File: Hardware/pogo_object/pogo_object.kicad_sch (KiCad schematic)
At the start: 32 parts, among them J1 10132797-035100LF, J2 10132797-015100LF, J3 Conn_01x02_Male, J4 Conn_01x02_Male, J5 Conn_01x04_Male, U1 dfr0489, U2 BSR802NL6327HTSA1, U3 mcp1407, U4 BSR802NL6327HTSA1

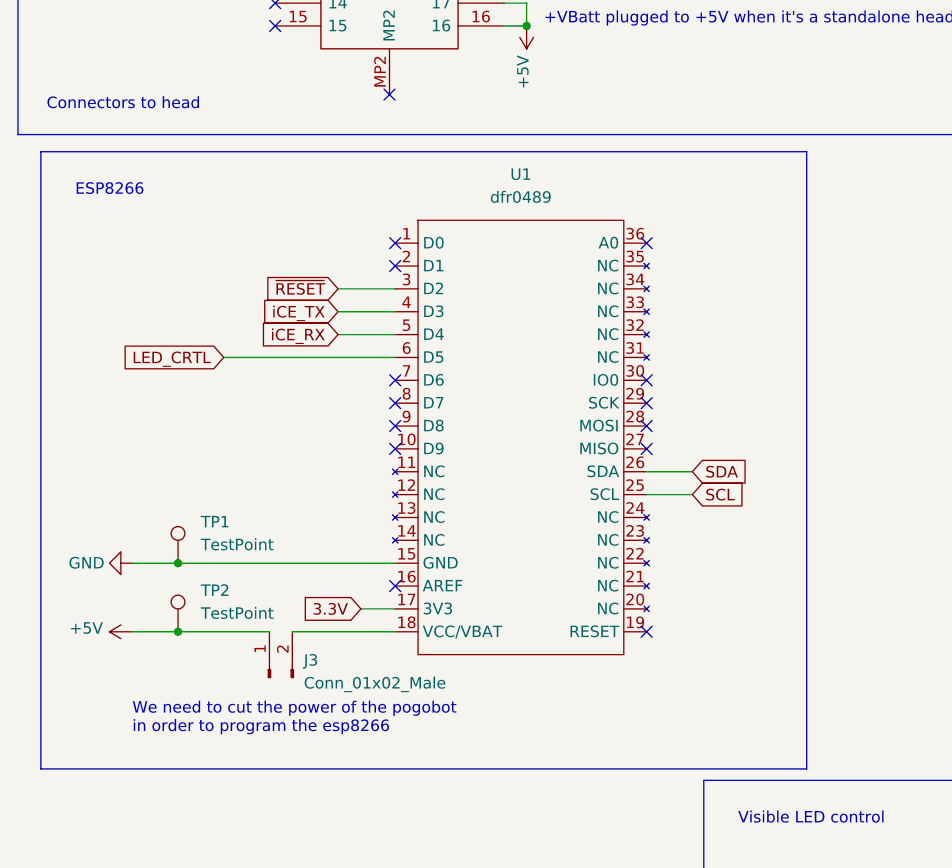
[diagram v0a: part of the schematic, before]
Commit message: adding battery voltage monitoring
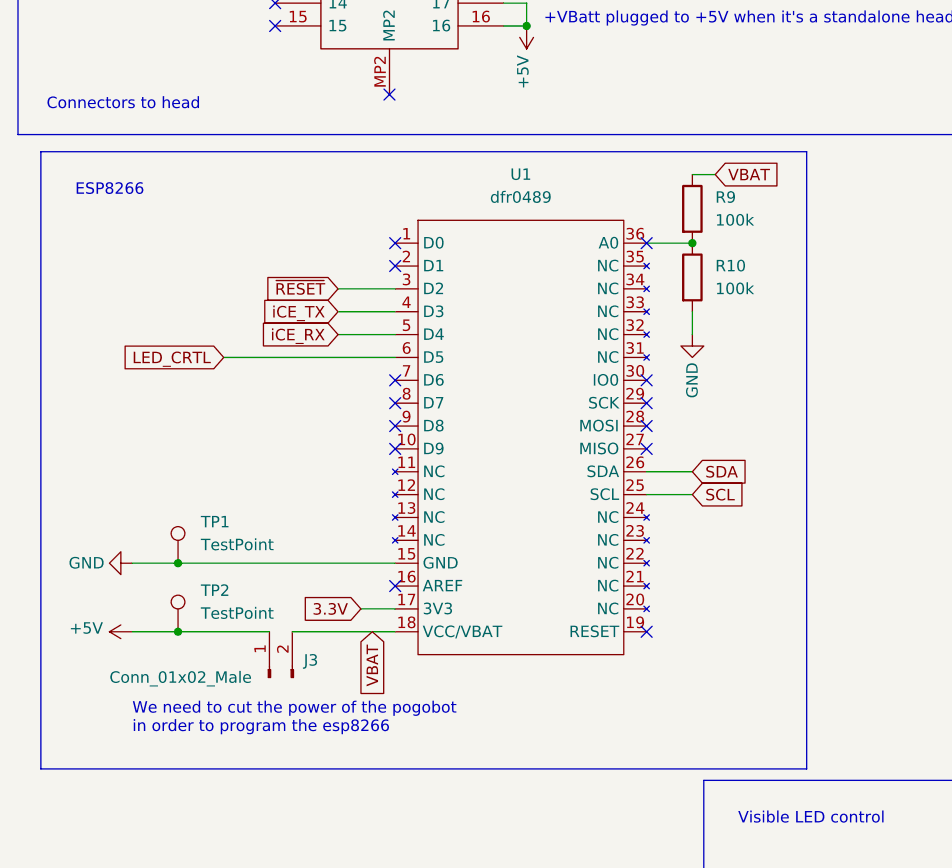
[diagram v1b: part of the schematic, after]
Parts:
- added R10, R9: 100k, Resistor_SMD:R_0805_2012Metric_Pad1.20x1.40mm_HandSolder, symbol Device:R
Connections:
- net GND: now also R10.2
- net VBAT: now reaches J3.2 (Pin_2), U1.18 (VCC/VBAT)
- net VBAT: now also R9.1
- net at U1.36 (A0): now also R10.1, R9.2
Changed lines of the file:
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@@
   (junction (at 31.75 124.46) (diameter 0) (color 0 0 0 0)
+  )
+  (junction (at 88.9 88.9) (diameter 0) (color 0 0 0 0)
   )
   (junction (at 201.93 113.03) (diameter 0) (color 0 0 0 0)
@@
     (stroke (width 0) (type default) (color 0 0 0 0))
   )
+  (wire (pts (xy 83.82 88.9) (xy 88.9 88.9))
+    (stroke (width 0) (type default) (color 0 0 0 0))
+  )
   (wire (pts (xy 76.2 31.75) (xy 67.945 31.75))
     (stroke (width 0) (type default) (color 0 0 0 0))
@@
     (stroke (width 0) (type default) (color 0 0 0 0))
   )
+  (wire (pts (xy 88.9 96.52) (xy 88.9 99.06))
+    (stroke (width 0) (type default) (color 0 0 0 0))
+  )
   (wire (pts (xy 76.2 36.83) (xy 67.945 36.83))
     (stroke (width 0) (type default) (color 0 0 0 0))
@@
   )
   (wire (pts (xy 31.75 132.08) (xy 41.91 132.08))
+    (stroke (width 0) (type default) (color 0 0 0 0))
+  )
+  (wire (pts (xy 88.9 81.28) (xy 91.44 81.28))
     (stroke (width 0) (type default) (color 0 0 0 0))
   )
@@
     )
   )
+  (global_label "VBAT" (shape input) (at 91.44 81.28 0) (fields_autoplaced)
+    (effects (font (size 1.27 1.27)) (justify left))
+    (property "Références Inter-Feuilles" "${INTERSHEET_REFS}" (id 0) (at 98.2679 81.3594 0)
+      (effects (font (size 1.27 1.27)) (justify left) hide)
+    )
+  )
   (global_label "SDA" (shape input) (at 185.42 31.75 0) (fields_autoplaced)
     (effects (font (size 1.27 1.27)) (justify left))
@@
     )
   )
+  (global_label "VBAT" (shape input) (at 53.34 132.08 270) (fields_autoplaced)
+    (effects (font (size 1.27 1.27)) (justify right))
+    (property "Références Inter-Feuilles" "${INTERSHEET_REFS}" (id 0) (at 53.2606 138.9079 90)
+      (effects (font (size 1.27 1.27)) (justify right) hide)
+    )
+  )
   (global_label "RGB_LED_IN" (shape input) (at 71.755 49.53 0) (fields_autoplaced)
     (effects (font (size 1.27 1.27)) (justify left))
@@
     )
     (property "Datasheet" "~" (id 3) (at 140.97 162.56 0)
+      (effects (font (size 1.27 1.27)) hide)
+    )
+    (pin "1")
+    (pin "2")
+  )
+  (symbol (lib_id "Device:R") (at 88.9 85.09 0) (unit 1)
+    (in_bom yes) (on_board yes) (fields_autoplaced)
+    (property "Reference" "R9" (id 0) (at 91.44 83.8199 0)
+      (effects (font (size 1.27 1.27)) (justify left))
+    )
+    (property "Value" "100k" (id 1) (at 91.44 86.3599 0)
+      (effects (font (size 1.27 1.27)) (justify left))
+    )
+    (property "Footprint" "Resistor_SMD:R_0805_2012Metric_Pad1.20x1.40mm_HandSolder" (id 2) (at 87.122 85.09 90)
+      (effects (font (size 1.27 1.27)) hide)
+    )
+    (property "Datasheet" "~" (id 3) (at 88.9 85.09 0)
       (effects (font (size 1.27 1.27)) hide)
     )
@@
     (pin "MP2")
   )
+  (symbol (lib_id "power:GND") (at 88.9 99.06 0) (mirror y) (unit 1)
+    (in_bom yes) (on_board yes)
+    (property "Reference" "#PWR014" (id 0) (at 88.9 105.41 0)
+      (effects (font (size 1.27 1.27)) hide)
+    )
+    (property "Value" "GND" (id 1) (at 88.9 104.14 90))
+    (property "Footprint" "" (id 2) (at 88.9 99.06 0)
+      (effects (font (size 1.27 1.27)) hide)
+    )
+    (property "Datasheet" "" (id 3) (at 88.9 99.06 0)
+      (effects (font (size 1.27 1.27)) hide)
+    )
+    (pin "1")
+  )
   (symbol (lib_id "Device:LED") (at 242.57 125.73 90) (unit 1)
     (in_bom yes) (on_board yes) (fields_autoplaced)
@@
   )
   (symbol (lib_id "Connector:Conn_01x02_Male") (at 41.91 137.16 90) (unit 1)
-    (in_bom yes) (on_board yes) (fields_autoplaced)
+    (in_bom yes) (on_board yes)
     (property "Reference" "J3" (id 0) (at 45.72 135.2549 90)
       (effects (font (size 1.27 1.27)) (justify right))
     )
-    (property "Value" "Conn_01x02_Male" (id 1) (at 45.72 137.7949 90)
+    (property "Value" "Conn_01x02_Male" (id 1) (at 24.13 137.16 90)
       (effects (font (size 1.27 1.27)) (justify right))
     )
@@
     (pin "1")
   )
+  (symbol (lib_id "Device:R") (at 88.9 92.71 0) (unit 1)
+    (in_bom yes) (on_board yes) (fields_autoplaced)
+    (property "Reference" "R10" (id 0) (at 91.44 91.4399 0)
+      (effects (font (size 1.27 1.27)) (justify left))
+    )
+    (property "Value" "100k" (id 1) (at 91.44 93.9799 0)
+      (effects (font (size 1.27 1.27)) (justify left))
+    )
+    (property "Footprint" "Resistor_SMD:R_0805_2012Metric_Pad1.20x1.40mm_HandSolder" (id 2) (at 87.122 92.71 90)
+      (effects (font (size 1.27 1.27)) hide)
+    )
+    (property "Datasheet" "~" (id 3) (at 88.9 92.71 0)
+      (effects (font (size 1.27 1.27)) hide)
+    )
+    (pin "1")
+    (pin "2")
+  )
   (symbol (lib_id "Connector:TestPoint") (at 31.75 132.08 0) (unit 1)
     (in_bom yes) (on_board yes) (fields_autoplaced)
@@
   (symbol (lib_id "power:+5V") (at 207.01 95.25 0) (unit 1)
     (in_bom yes) (on_board yes)
-    (property "Reference" "#PWR?" (id 0) (at 207.01 99.06 0)
+    (property "Reference" "#PWR016" (id 0) (at 207.01 99.06 0)
       (effects (font (size 1.27 1.27)) hide)
     )
@@
       (reference "#PWR013") (unit 1) (value "GND") (footprint "")
     )
+    (path "/455bcded-2079-44cc-83de-11d601fba79d"
+      (reference "#PWR014") (unit 1) (value "GND") (footprint "")
+    )
     (path "/c81b13d2-4906-4731-bb8e-7207c3e9467f"
       (reference "#PWR015") (unit 1) (value "+5V") (footprint "")
     )
     (path "/d647658c-bff2-4f7e-9eac-6ff0c562c1bf"
-      (reference "#PWR?") (unit 1) (value "+5V") (footprint "")
+      (reference "#PWR016") (unit 1) (value "+5V") (footprint "")
     )
     (path "/e79ac02e-4fa2-4af5-9bc2-526dddaaee9c"
@@
       (reference "R8") (unit 1) (value "36") (footprint "Resistor_SMD:R_0805_2012Metric_Pad1.20x1.40mm_HandSolder")
     )
+    (path "/1b9fd7d0-43b9-477a-81ed-a2adbb2b815c"
+      (reference "R9") (unit 1) (value "100k") (footprint "Resistor_SMD:R_0805_2012Metric_Pad1.20x1.40mm_HandSolder")
+    )
+    (path "/bfd86dc7-113a-45e7-b0f9-f3587781f21a"
+      (reference "R10") (unit 1) (value "100k") (footprint "Resistor_SMD:R_0805_2012Metric_Pad1.20x1.40mm_HandSolder")
+    )
     (path "/b9524c4e-a371-422a-8b41-0d93f0c42945"

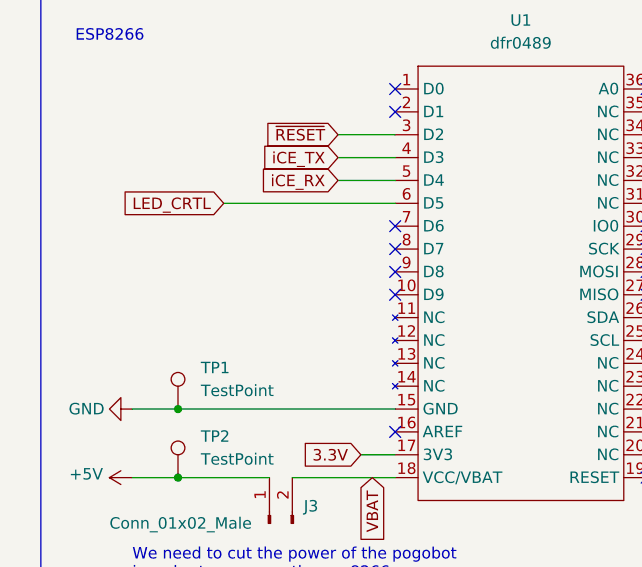
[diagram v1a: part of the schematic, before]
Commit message: updates the pogobject pcb to include config mode
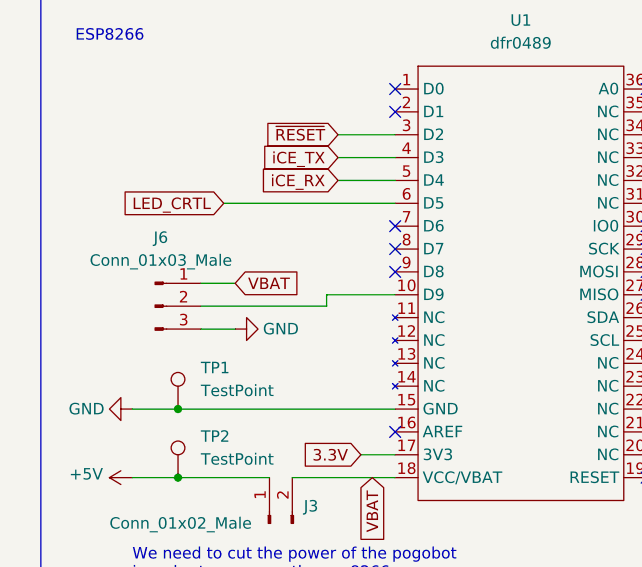
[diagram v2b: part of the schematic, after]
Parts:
- added J6: Conn_01x03_Male, Connector_PinHeader_2.54mm:PinHeader_1x03_P2.54mm_Vertical, symbol Connector:Conn_01x03_Male
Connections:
- net GND: now also J6.3 (Pin_3)
- net VBAT: now also J6.1 (Pin_1)
- net at U1.10 (D9): now also J6.2 (Pin_2)
- no-connect marks 29 -> 28
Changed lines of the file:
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@@
   (no_connect (at 138.43 40.64))
   (no_connect (at 42.545 57.15))
-  (no_connect (at 55.88 111.76))
   (no_connect (at 42.545 59.69))
   (no_connect (at 55.245 72.39))
@@
     (stroke (width 0) (type default) (color 0 0 0 0))
   )
+  (wire (pts (xy 34.29 110.49) (xy 38.1 110.49))
+    (stroke (width 0) (type default) (color 0 0 0 0))
+  )
   (wire (pts (xy 110.49 40.64) (xy 113.03 40.64))
     (stroke (width 0) (type default) (color 0 0 0 0))
@@
     (stroke (width 0) (type default) (color 0 0 0 0))
   )
+  (wire (pts (xy 34.29 113.03) (xy 48.26 113.03))
+    (stroke (width 0) (type default) (color 0 0 0 0))
+  )
   (wire (pts (xy 203.2 146.05) (xy 208.28 146.05))
     (stroke (width 0) (type default) (color 0 0 0 0))
   )
+  (wire (pts (xy 48.26 113.03) (xy 48.26 111.76))
+    (stroke (width 0) (type default) (color 0 0 0 0))
+  )
   (wire (pts (xy 37.465 31.75) (xy 42.545 31.75))
     (stroke (width 0) (type default) (color 0 0 0 0))
@@
   )
   (polyline (pts (xy 170.18 165.1) (xy 170.18 73.66))
+    (stroke (width 0) (type default) (color 0 0 0 0))
+  )
+  (wire (pts (xy 34.29 115.57) (xy 38.1 115.57))
+    (stroke (width 0) (type default) (color 0 0 0 0))
+  )
+  (wire (pts (xy 48.26 111.76) (xy 55.88 111.76))
     (stroke (width 0) (type default) (color 0 0 0 0))
   )
@@
     (property "Références Inter-Feuilles" "${INTERSHEET_REFS}" (id 0) (at 25.4664 101.5206 0)
       (effects (font (size 1.27 1.27)) (justify right) hide)
+    )
+  )
+  (global_label "VBAT" (shape input) (at 38.1 110.49 0) (fields_autoplaced)
+    (effects (font (size 1.27 1.27)) (justify left))
+    (property "Références Inter-Feuilles" "${INTERSHEET_REFS}" (id 0) (at 44.9279 110.5694 0)
+      (effects (font (size 1.27 1.27)) (justify left) hide)
     )
   )
@@
     (pin "1")
   )
+  (symbol (lib_id "power:GND") (at 38.1 115.57 90) (mirror x) (unit 1)
+    (in_bom yes) (on_board yes)
+    (property "Reference" "#PWR017" (id 0) (at 44.45 115.57 0)
+      (effects (font (size 1.27 1.27)) hide)
+    )
+    (property "Value" "GND" (id 1) (at 43.18 115.57 90))
+    (property "Footprint" "" (id 2) (at 38.1 115.57 0)
+      (effects (font (size 1.27 1.27)) hide)
+    )
+    (property "Datasheet" "" (id 3) (at 38.1 115.57 0)
+      (effects (font (size 1.27 1.27)) hide)
+    )
+    (pin "1")
+  )
   (symbol (lib_id "power:+5V") (at 135.89 157.48 0) (unit 1)
     (in_bom yes) (on_board yes)
@@
     (pin "1")
     (pin "2")
+  )
+  (symbol (lib_id "Connector:Conn_01x03_Male") (at 29.21 113.03 0) (unit 1)
+    (in_bom yes) (on_board yes) (fields_autoplaced)
+    (property "Reference" "J6" (id 0) (at 29.845 105.41 0))
+    (property "Value" "Conn_01x03_Male" (id 1) (at 29.845 107.95 0))
+    (property "Footprint" "Connector_PinHeader_2.54mm:PinHeader_1x03_P2.54mm_Vertical" (id 2) (at 29.21 113.03 0)
+      (effects (font (size 1.27 1.27)) hide)
+    )
+    (property "Datasheet" "~" (id 3) (at 29.21 113.03 0)
+      (effects (font (size 1.27 1.27)) hide)
+    )
+    (pin "1")
+    (pin "2")
+    (pin "3")
   )
   (symbol (lib_id "bsr802:BSR802NL6327HTSA1") (at 128.27 173.99 0) (unit 1)
@@
       (reference "#PWR016") (unit 1) (value "+5V") (footprint "")
     )
+    (path "/678ebcf8-7b90-405d-804f-661653c971f2"
+      (reference "#PWR017") (unit 1) (value "GND") (footprint "")
+    )
     (path "/e79ac02e-4fa2-4af5-9bc2-526dddaaee9c"
       (reference "C1") (unit 1) (value "1uF") (footprint "Capacitor_THT:CP_Radial_D8.0mm_P5.00mm")
@@
       (reference "J5") (unit 1) (value "Conn_01x04_Male") (footprint "Connector_PinHeader_2.54mm:PinHeader_1x04_P2.54mm_Vertical")
     )
+    (path "/6e2607a0-a356-4c92-bef7-2294449cd8b1"
+      (reference "J6") (unit 1) (value "Conn_01x03_Male") (footprint "Connector_PinHeader_2.54mm:PinHeader_1x03_P2.54mm_Vertical")
+    )
     (path "/263dd3c5-854c-4998-b01d-4eeae0360868"
